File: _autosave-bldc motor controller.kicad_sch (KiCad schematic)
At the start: 48 parts, among them J1 Conn_01x04_Pin, U1 C47023655, U3 C529358, U6 C126671

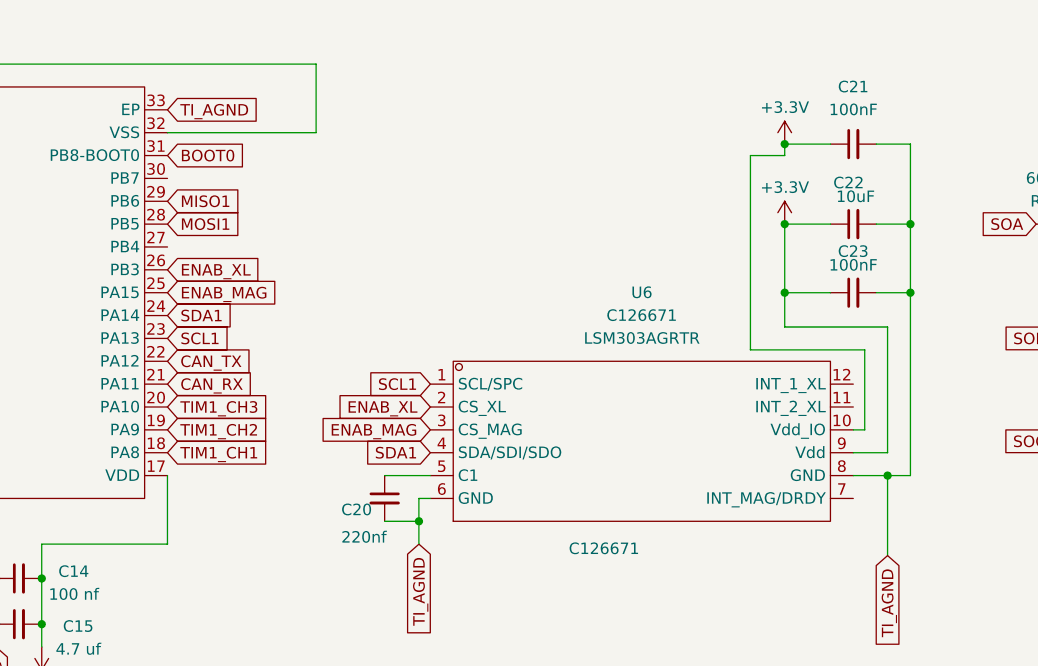
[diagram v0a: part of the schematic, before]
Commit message: updated certain capacitor sizes, doubled power vias for saftey
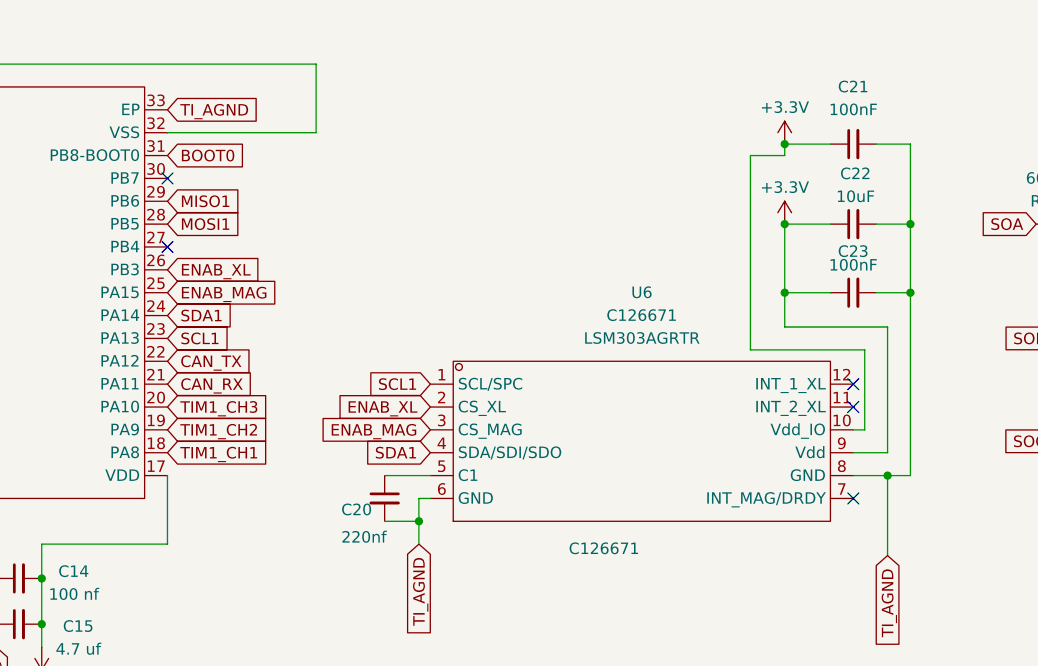
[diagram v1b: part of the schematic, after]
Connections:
- no-connect marks 12 -> 17
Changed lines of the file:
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@@
 	)
 	(no_connect
+		(at 148.59 72.39)
+	)
+	(no_connect
 		(at 64.77 140.97)
 	)
@@
 	)
 	(no_connect
+		(at 148.59 82.55)
+	)
+	(no_connect
+		(at 72.39 46.99)
+	)
+	(no_connect
 		(at 41.91 128.27)
 	)
 	(no_connect
+		(at 148.59 69.85)
+	)
+	(no_connect
 		(at 41.91 125.73)
 	)
+	(no_connect
+		(at 72.39 54.61)
+	)
 	(wire
 		(pts
@@
 		(dnp no)
 		(property "Reference" "C22"
-			(at 148.082 47.498 90)
+			(at 148.844 46.482 90)
 			(effects
 				(font
